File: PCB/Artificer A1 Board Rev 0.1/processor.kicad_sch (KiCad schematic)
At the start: 1 part, among them U1 T527M00X0DCH

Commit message: schematic update
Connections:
- net DP: now reaches U1.A24 (USB0-DP)
- net DM: now reaches U1.B24 (USB0-DM)
- net USB1-DP: now reaches U1.D24 (USB1-DP)
- net USB1-DM: now reaches U1.E24 (USB1-DM)
- net PCIE-TX0-DP/USB3-TXP : now reaches U1.A22 (PCIETX0-DP/USB)
- net PCIE-REF-CLKP: now reaches U1.B21 (PCIEREFCLKP)
- net PCIE-TX0-DN/USB3-TXN: now reaches U1.B22 (PCIETX0-DN/USB)
- net PCIE-RX0-DP/USB3-RXP: now reaches U1.B23 (PCIERX0-DP/US)
- net PCIE-REF-CLKN: now reaches U1.C21 (PCIEREFCLKN)
- net PCIE-RX0-DN/USB3-RXN: now reaches U1.C23 (PCIERX0-DN/US)
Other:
- moved on the sheet: U1D

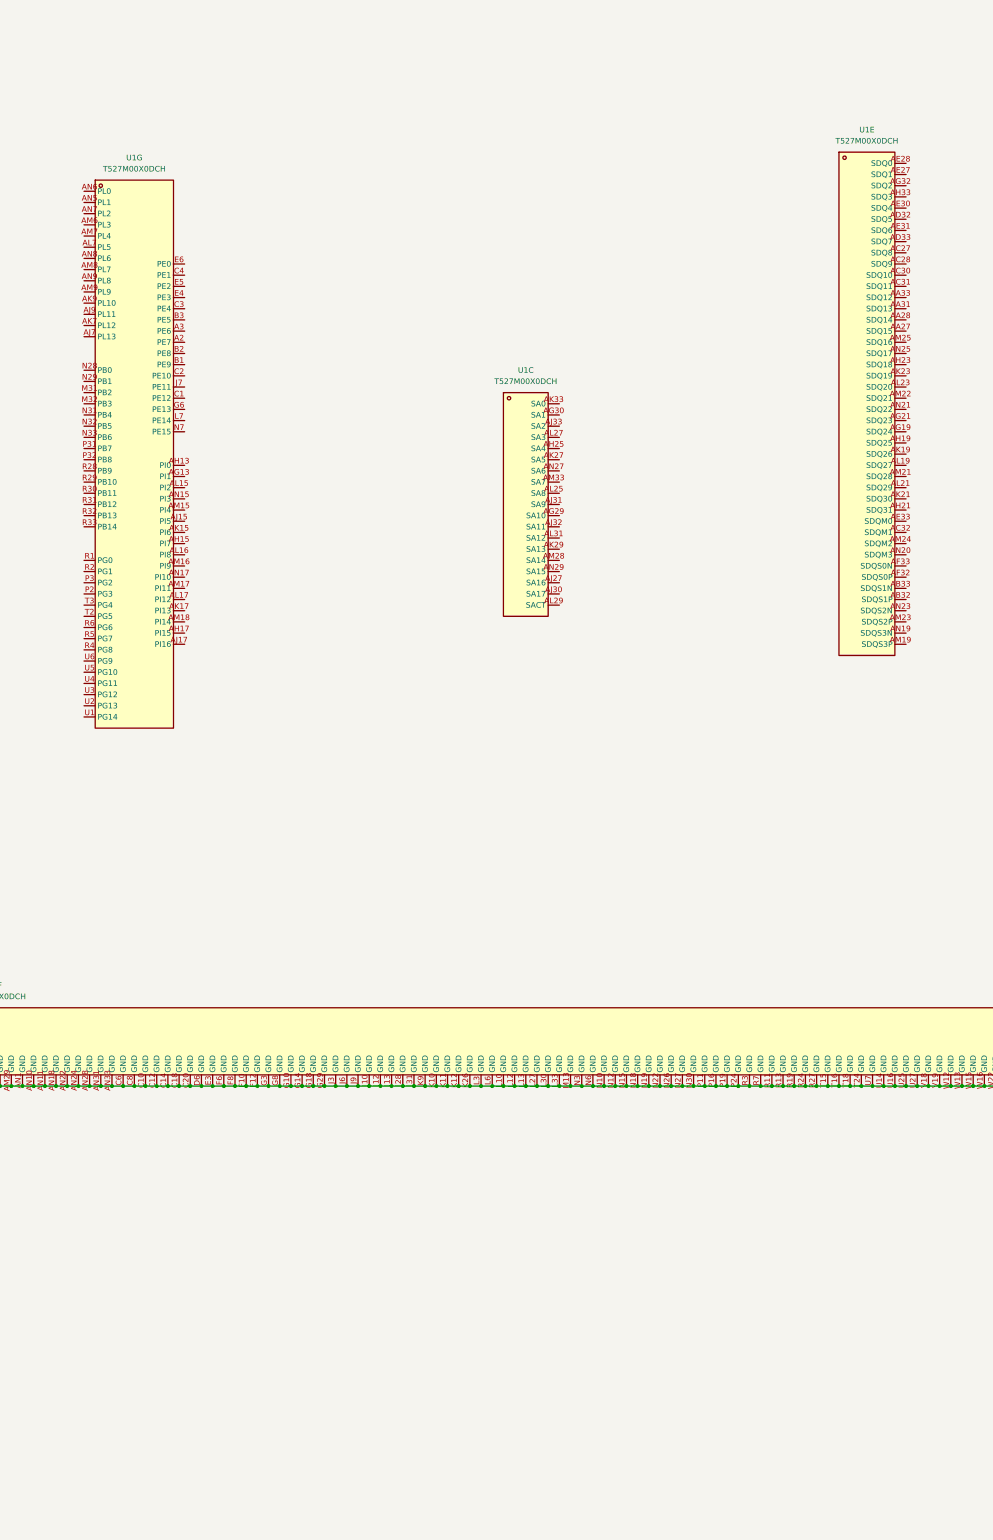
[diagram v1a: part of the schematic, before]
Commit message: localized libraries
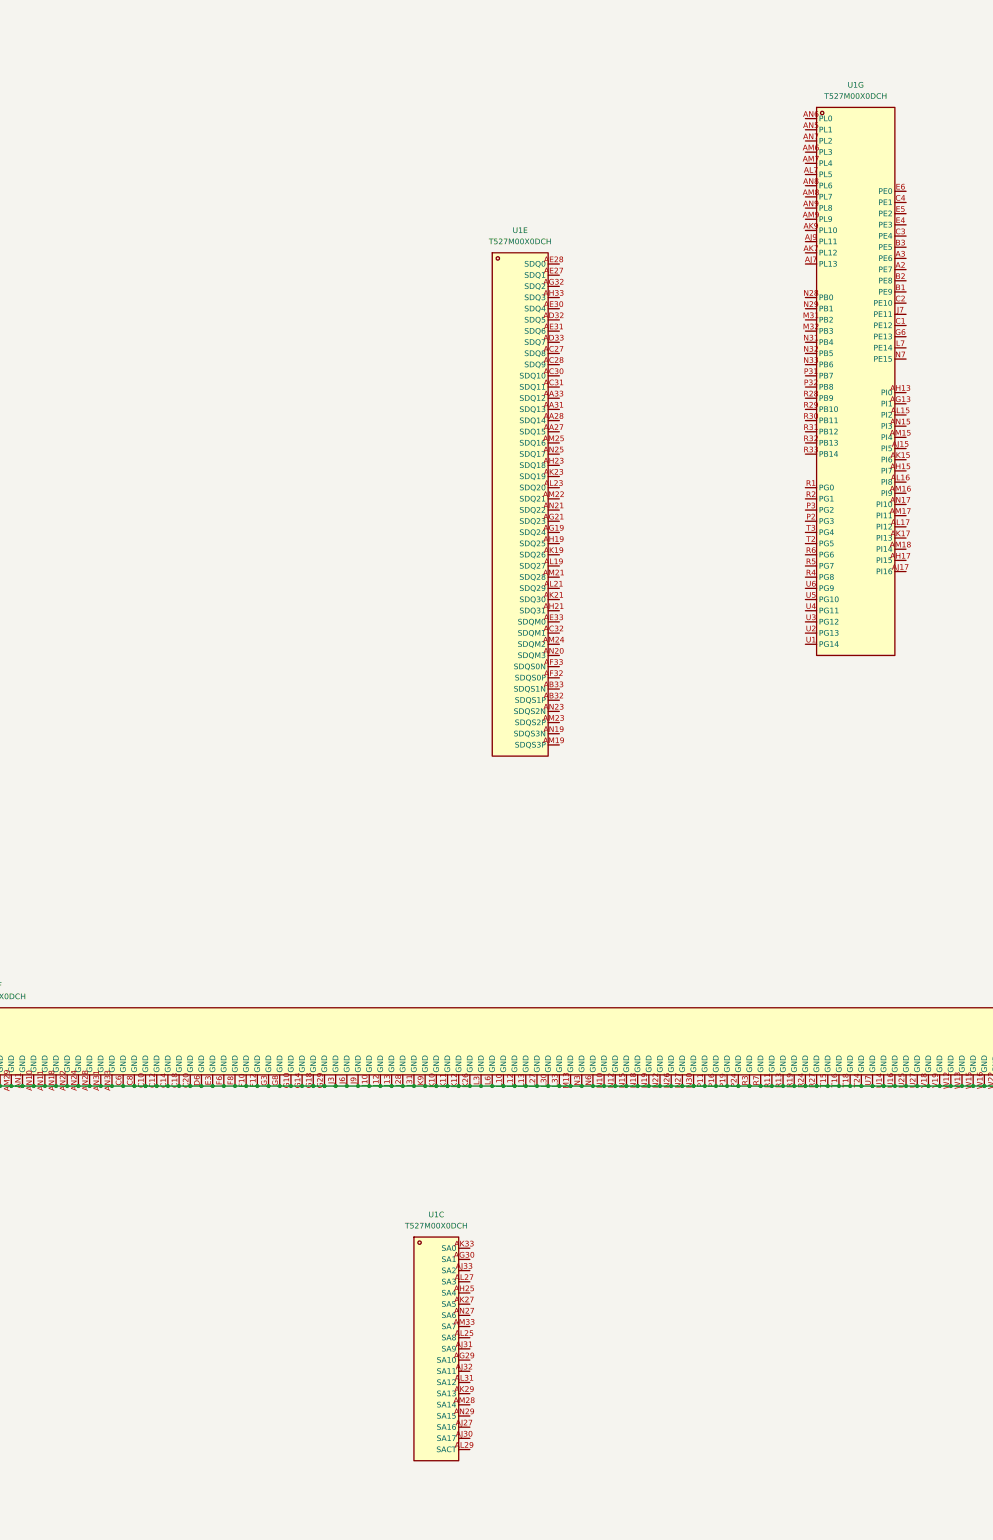
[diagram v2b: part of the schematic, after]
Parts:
- removed U1: T527M00X0DCH, easyeda2kicad:BGA-664_L17.0-W17.0_T527, symbol easyeda2kicad:T527M00X0DCH
- added U1: T527M00X0DCH, easyeda:BGA-664_L17.0-W17.0_T527, symbol easyeda:T527M00X0DCH
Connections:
- net AGND: now also U1.AE3 (AGND)
- net AVSS: now also U1.A32 (AVSS), U1.A33 (AVSS), U1.C22 (AVSS), U1.C24 (AVSS), U1.C26 (AVSS), U1.C28 (AVSS), U1.C30 (AVSS), U1.C31 (AVSS), U1.E29 (AVSS), U1.F22 (AVSS), U1.F24 (AVSS), U1.G26 (AVSS), U1.G28 (AVSS), U1.H24 (AVSS), U1.J17 (AVSS), U1.J21 (AVSS), U1.J22 (AVSS), U1.J23 (AVSS), U1.J26 (AVSS), U1.K15 (AVSS), U1.K16 (AVSS), U1.K21 (AVSS), U1.K22 (AVSS), U1.K24 (AVSS), U1.K25 (AVSS), U1.L16 (AVSS), U1.L19 (AVSS), U1.L24 (AVSS), U1.M16 (AVSS), U1.M18 (AVSS), U1.M19 (AVSS)
- net DM: now also U1.B24 (USB0-DM)
- net DP: now also U1.A24 (USB0-DP)
- net GND: now also U1.A1 (GND), U1.AA15 (GND), U1.AA16 (GND), U1.AA18 (GND), U1.AA21 (GND), U1.AA22 (GND), U1.AA26 (GND), U1.AA30 (GND), U1.AA32 (GND), U1.AB10 (GND), U1.AB11 (GND), U1.AB12 (GND), U1.AB14 (GND), U1.AB15 (GND), U1.AB17 (GND), U1.AC1 (GND), U1.AC26 (GND), U1.AC29 (GND), U1.AC33 (GND), U1.AD11 (GND), U1.AD13 (GND), U1.AD14 (GND), U1.AD20 (GND), U1.AD21 (GND), U1.AD22 (GND), U1.AD9 (GND), U1.AE12 (GND), U1.AE14 (GND), U1.AE18 (GND), U1.AE19 (GND), U1.AE20 (GND), U1.AE21 (GND), U1.AE22 (GND), U1.AE23 (GND), U1.AE24 (GND), U1.AE25 (GND), U1.AE26 (GND), U1.AE29 (GND), U1.AE32 (GND), U1.AE9 (GND), U1.AG11 (GND), U1.AG25 (GND), U1.AG28 (GND), U1.AG3 (GND), U1.AG31 (GND), U1.AG33 (GND), U1.AG6 (GND), U1.AG7 (GND), U1.AH27 (GND), U1.AH32 (GND), U1.AH7 (GND), U1.AH9 (GND), U1.AJ13 (GND), U1.AJ19 (GND), U1.AJ21 (GND), U1.AJ23 (GND), U1.AK11 (GND), U1.AK32 (GND), U1.AK5 (GND), U1.AL12 (GND), U1.AL13 (GND), U1.AL14 (GND), U1.AL3 (GND), U1.AL9 (GND), U1.AM20 (GND), U1.AM26 (GND), U1.AM29 (GND), U1.AM5 (GND), U1.AN1 (GND), U1.AN10 (GND), U1.AN11 (GND), U1.AN18 (GND), U1.AN22 (GND), U1.AN24 (GND), U1.AN28 (GND), U1.AN31 (GND), U1.AN33 (GND), U1.C10 (GND), U1.C12 (GND), U1.C14 (GND), U1.C18 (GND), U1.C20 (GND), U1.C6 (GND), U1.C8 (GND), U1.D6 (GND), U1.E3 (GND), U1.F10 (GND), U1.F12 (GND), U1.F6 (GND), U1.F8 (GND), U1.G10 (GND), U1.G14 (GND), U1.G18 (GND), U1.G29 (GND), U1.G3 (GND), U1.G8 (GND), U1.J10 (GND), U1.J12 (GND), U1.J13 (GND), U1.J28 (GND), U1.J3 (GND), U1.J31 (GND), U1.J6 (GND), U1.J9 (GND), U1.K10 (GND), U1.K11 (GND), U1.K12 (GND), U1.K26 (GND), U1.K9 (GND), U1.L10 (GND), U1.L12 (GND), U1.L13 (GND), U1.L27 (GND), U1.L3 (GND), U1.L30 (GND), U1.L33 (GND), U1.L6 (GND), U1.M13 (GND), U1.N10 (GND), U1.N12 (GND), U1.N15 (GND), U1.N18 (GND), U1.N19 (GND), U1.N22 (GND), U1.N26 (GND), U1.N27 (GND), U1.N3 (GND), U1.N30 (GND), U1.N6 (GND), U1.P11 (GND), U1.P16 (GND), U1.P19 (GND), U1.P24 (GND), U1.R11 (GND), U1.R13 (GND), U1.R19 (GND), U1.R24 (GND), U1.R27 (GND), U1.R3 (GND), U1.R7 (GND), U1.T15 (GND), U1.T16 (GND), U1.T18 (GND), U1.T24 (GND), U1.U14 (GND), U1.U16 (GND), U1.U25 (GND), U1.U27 (GND), U1.U7 (GND), U1.V18 (GND), U1.V19 (GND), U1.W12 (GND), U1.W13 (GND), U1.W15 (GND), U1.W16 (GND), U1.W22 (GND), U1.W27 (GND), U1.W30 (GND), U1.Y15 (GND), U1.Y18 (GND), U1.Y22 (GND), U1.Y23 (GND), U1.Y26 (GND)
- net GNDADC: now also U1.AA7 (GNDADC)
- net PCIE-REF-CLKN: now also U1.C21 (PCIEREFCLKN)
- net PCIE-REF-CLKP: now also U1.B21 (PCIEREFCLKP)
- net PCIE-RX0-DN/USB3-RXN: now also U1.C23 (PCIERX0-DN/US)
- net PCIE-RX0-DP/USB3-RXP: now also U1.B23 (PCIERX0-DP/US)
- net PCIE-TX0-DN/USB3-TXN: now also U1.B22 (PCIETX0-DN/USB)
- net PCIE-TX0-DP/USB3-TXP : now also U1.A22 (PCIETX0-DP/USB)
- net USB1-DM: now also U1.E24 (USB1-DM)
- net USB1-DP: now also U1.D24 (USB1-DP)
- new net: U1.AA12 (VDDDNR), U1.AA13 (VDDDNR), U1.Y12 (VDDDNR), U1.Y13 (VDDDNR)
- new net: U1.AA24 (VCCDRAM), U1.AB24 (VCCDRAM), U1.AC24 (VCCDRAM), U1.W23 (VCCDRAM), U1.W24 (VCCDRAM), U1.W25 (VCCDRAM), U1.Y24 (VCCDRAM)
- new net: U1.AC17 (VCCDRAML), U1.AC18 (VCCDRAML), U1.AC19 (VCCDRAML), U1.AC20 (VCCDRAML), U1.AC22 (VCCDRAML)
- new net: U1.N21 (VDDDE), U1.P21 (VDDDE)
- new net: U1.T11 (VDDGPU), U1.T13 (VDDGPU), U1.U12 (VDDGPU), U1.U13 (VDDGPU)
- new net: U1.T19 (VDDCPUB), U1.T21 (VDDCPUB), U1.T22 (VDDCPUB), U1.U18 (VDDCPUB), U1.U19 (VDDCPUB), U1.U21 (VDDCPUB), U1.U22 (VDDCPUB)
- new net: U1.W19 (VDDCPUL), U1.W21 (VDDCPUL), U1.Y19 (VDDCPUL), U1.Y21 (VDDCPUL)

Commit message: added a few accessories
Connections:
- net MCSIA-CKN: now reaches U1.A10 (PK4)
- net MCSIA-D0N: now reaches U1.A12 (PK0)
- net RGMII0-TXD2: now reaches U1.A14 (PH18)
- net MCSID-CKN: now reaches U1.A4 (PK22)
- net MCSID-D1N: now reaches U1.A5 (PK20)
- net MCSID-D0N: now reaches U1.A6 (PK18)
- net MCSIC-D1N: now reaches U1.A8 (PK14)
- net MCSIA-CKP: now reaches U1.B10 (PK5)
- net MCSIA-D1N: now reaches U1.B11 (PK2)
- net MCSIA-D0P: now reaches U1.B12 (PK1)
- net RGMII0-TXD3: now reaches U1.B13 (PH17)
- net RGMII0-RXCK: now reaches U1.B14 (PH16)
- net RGMII0-MDIO: now reaches U1.B16 (PH10)
- net RGMII0-TXD1: now reaches U1.B17 (PH4)
- net MCSID-CKP: now reaches U1.B4 (PK23)
- net MCSID-D1P: now reaches U1.B5 (PK21)
- net MCSID-D0P: now reaches U1.B6 (PK19)
- net MCSIC-CKN: now reaches U1.B7 (PK16)
- net MCSIC-D1P: now reaches U1.B8 (PK15)
- net MCSIC-D0N: now reaches U1.B9 (PK12)
- net MCSIA-D1P: now reaches U1.C11 (PK3)
- net RGMII0-MDC: now reaches U1.C16 (PH9)
- net RGMII0-CLKIN: now reaches U1.C17 (PH3)
- net MCSIC-CKP: now reaches U1.C7 (PK17)
- net MCSIC-D0P: now reaches U1.C9 (PK13)
- net RGMII1-RXD1: now reaches U1.D1 (PJ0)
- net MCSIB-D1P: now reaches U1.D10 (PK9)
- net MCSIB-D0P: now reaches U1.D12 (PK7)
- net RGMII0-RXD2: now reaches U1.D14 (PH15)
- net RGMII0-RXCTL: now reaches U1.D18 (PH2)
- net RGMII1-RXD0: now reaches U1.D2 (PJ1)
- net RGMII1-RXD0: now also U1.F2 (PJ5)
- net MCSIB-CKP: now reaches U1.D8 (PK11)
- net RGMII1-RXCTL: now reaches U1.E1 (PJ2)
- net MCSIB-D1N: now reaches U1.E10 (PK8)
- net MCSIB-D0N: now reaches U1.E12 (PK6)
- net RGMII0-RXD3: now reaches U1.E14 (PH14)
- net RGMII0-TXD0: now reaches U1.E16 (PH5)
- net RGMII0-RXD0: now reaches U1.E18 (PH1)
- net RGMII1-CLKIN: now reaches U1.E2 (PJ3)
- net MCSIB-CKN: now reaches U1.E8 (PK10)
- net RGMII1-TXD1: now reaches U1.F1 (PJ4)
- net RGMII0-TXCTL: now reaches U1.F14 (PH7)
- net RGMII0-RXD1: now reaches U1.F18 (PH0)
- net RGMII1-TXCK: now reaches U1.G1 (PJ6)
- net RGMII0-TXCK: now reaches U1.G12 (PH6)
- net RGMII1-TXCTL: now reaches U1.G2 (PJ7)
- net RGMII1-RXD3: now reaches U1.G5 (PJ11)
- net RGMII1-MDC: now reaches U1.H2 (PJ8)
- net RGMII1-MDIO: now reaches U1.H3 (PJ9)
- net RGMII1-RXD2: now reaches U1.J4 (PJ12)
- net RGMII1-RXCK: now reaches U1.J5 (PJ13)
- net RGMII1-TXD3: now reaches U1.L4 (PJ14)
- net RGMII1-TXD2: now reaches U1.L5 (PJ15)
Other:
- moved on the sheet: U1A, U1D, U1E, U1G

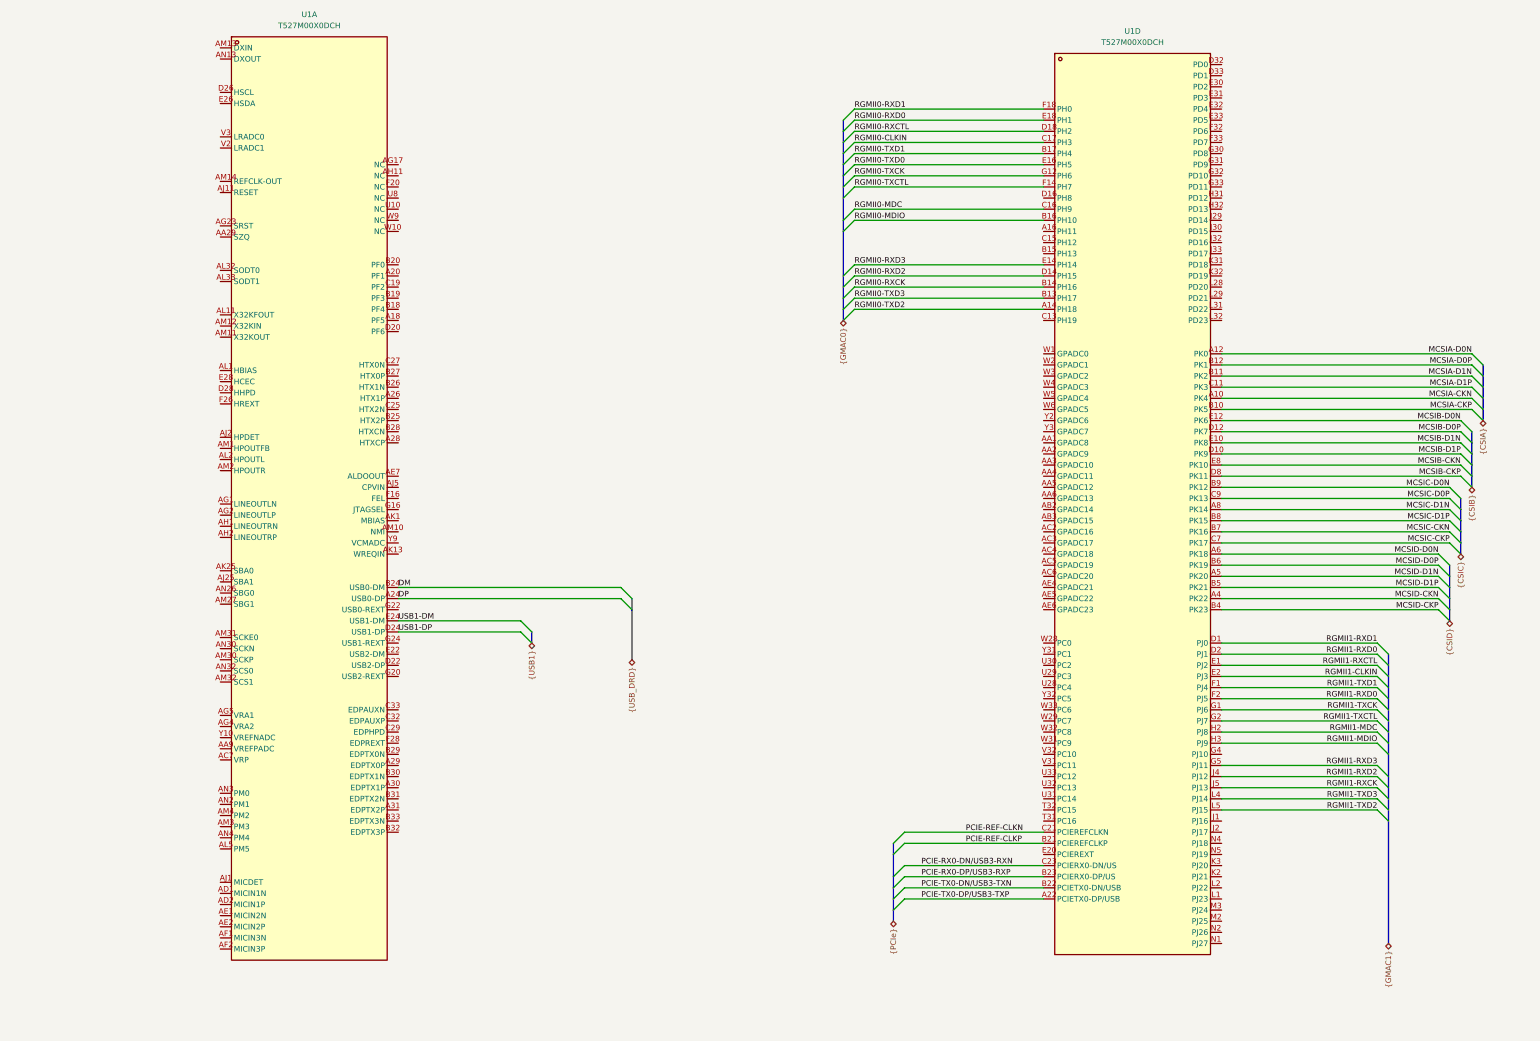
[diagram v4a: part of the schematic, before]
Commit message: added HDMI, DP, DSI, etc
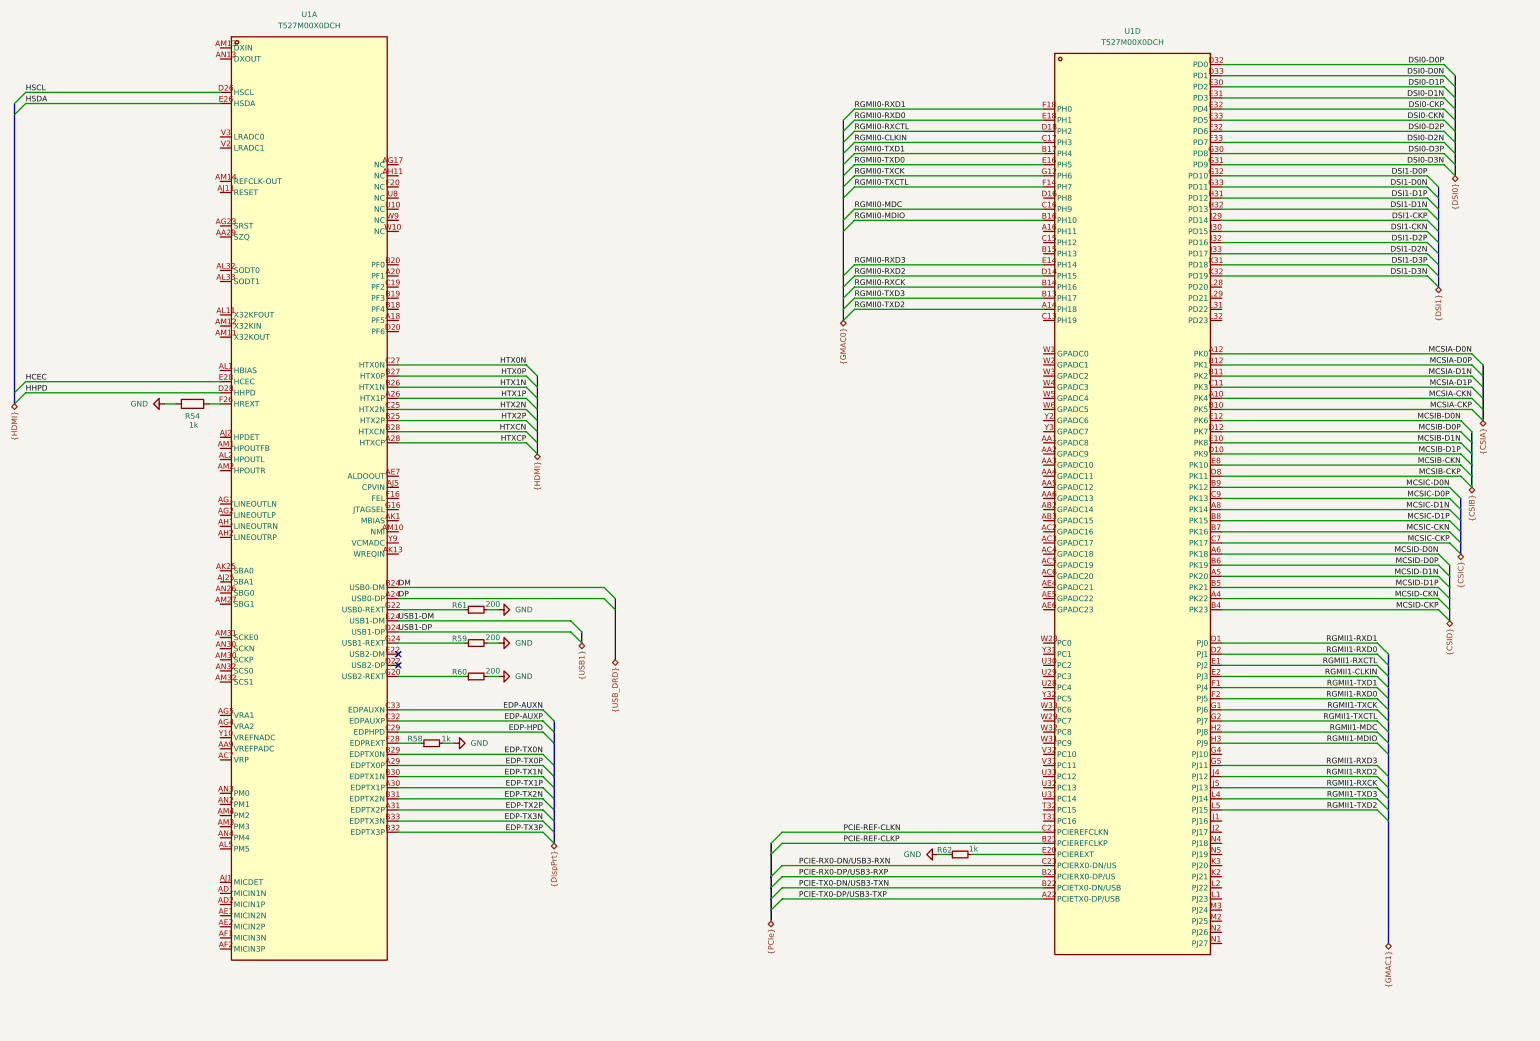
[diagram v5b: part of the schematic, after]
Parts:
- added R54: 1k, symbol Device:R
- added R58, R62: 1k, symbol Device:R_Small
- added R59, R60, R61: 200, symbol Device:R_Small
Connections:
- net GND: now also R54.1, R58.2, R59.2, R60.2, R61.2, R62.1
- net DSI0-D0P: now reaches U1.D32 (PD0)
- net DSI0-D0N: now reaches U1.D33 (PD1)
- net at U1.E20 (PCIEREXT): now also R62.2
- net DSI0-D1P: now reaches U1.E30 (PD2)
- net DSI0-D1N: now reaches U1.E31 (PD3)
- net DSI0-CKP: now reaches U1.E32 (PD4)
- net DSI0-CKN: now reaches U1.E33 (PD5)
- net DSI0-D2P: now reaches U1.F32 (PD6)
- net DSI0-D2N: now reaches U1.F33 (PD7)
- net DSI0-D3P: now reaches U1.G30 (PD8)
- net DSI0-D3N: now reaches U1.G31 (PD9)
- net DSI1-D0P: now reaches U1.G32 (PD10)
- net DSI1-D0N: now reaches U1.G33 (PD11)
- net DSI1-D1P: now reaches U1.H31 (PD12)
- net DSI1-D1N: now reaches U1.H32 (PD13)
- net DSI1-CKP: now reaches U1.J29 (PD14)
- net DSI1-CKN: now reaches U1.J30 (PD15)
- net DSI1-D2P: now reaches U1.J32 (PD16)
- net DSI1-D2N: now reaches U1.J33 (PD17)
- net DSI1-D3P: now reaches U1.K31 (PD18)
- net DSI1-D3N: now reaches U1.K32 (PD19)
- net HTX1P: now reaches U1.A26 (HTX1P)
- net HTXCP: now reaches U1.A28 (HTXCP)
- net EDP-TX0P: now reaches U1.A29 (EDPTX0P)
- net EDP-TX1P: now reaches U1.A30 (EDPTX1P)
- net EDP-TX2P: now reaches U1.A31 (EDPTX2P)
- net HTX2P: now reaches U1.B25 (HTX2P)
- net HTX1N: now reaches U1.B26 (HTX1N)
- net HTX0P: now reaches U1.B27 (HTX0P)
- net HTXCN: now reaches U1.B28 (HTXCN)
- net EDP-TX0N: now reaches U1.B29 (EDPTX0N)
- net EDP-TX1N: now reaches U1.B30 (EDPTX1N)
- net EDP-TX2N: now reaches U1.B31 (EDPTX2N)
- net EDP-TX3P: now reaches U1.B32 (EDPTX3P)
- net EDP-TX3N: now reaches U1.B33 (EDPTX3N)
- net HTX2N: now reaches U1.C25 (HTX2N)
- net HTX0N: now reaches U1.C27 (HTX0N)
- net EDP-HPD: now reaches U1.C29 (EDPHPD)
- net EDP-AUXP: now reaches U1.C32 (EDPAUXP)
- net EDP-AUXN: now reaches U1.C33 (EDPAUXN)
- net HSCL: now reaches U1.D26 (HSCL)
- net HHPD: now reaches U1.D28 (HHPD)
- net HSDA: now reaches U1.E26 (HSDA)
- net HCEC: now reaches U1.E28 (HCEC)
- net at U1.F26 (HREXT): now also R54.2
- net at U1.F28 (EDPREXT): now also R58.1
- net at U1.G20 (USB2-REXT): now also R60.1
- net at U1.G22 (USB0-REXT): now also R61.1
- net at U1.G24 (USB1-REXT): now also R59.1
- no-connect marks 0 -> 2

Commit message: finished dram
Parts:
- removed unit 3 of U1
- removed unit 5 of U1
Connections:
- net AVSS is gone; now on net GND: U1.A32 (AVSS), U1.A33 (AVSS), U1.C22 (AVSS), U1.C24 (AVSS), U1.C26 (AVSS), U1.C28 (AVSS), U1.C30 (AVSS), U1.C31 (AVSS), U1.E29 (AVSS), U1.F22 (AVSS), U1.F24 (AVSS), U1.G26 (AVSS), U1.G28 (AVSS), U1.H24 (AVSS), U1.J17 (AVSS), U1.J21 (AVSS), U1.J22 (AVSS), U1.J23 (AVSS), U1.J26 (AVSS), U1.K15 (AVSS), U1.K16 (AVSS), U1.K21 (AVSS), U1.K22 (AVSS), U1.K24 (AVSS), U1.K25 (AVSS), U1.L16 (AVSS), U1.L19 (AVSS), U1.L24 (AVSS), U1.M16 (AVSS), U1.M18 (AVSS), U1.M19 (AVSS)
- net VDD11-DRAM: now reaches U1.AA24 (VCCDRAM), U1.AB24 (VCCDRAM), U1.AC24 (VCCDRAM), U1.W23 (VCCDRAM), U1.W24 (VCCDRAM), U1.W25 (VCCDRAM), U1.Y24 (VCCDRAM)
- net VDD06-DRAM: now reaches U1.AC17 (VCCDRAML), U1.AC18 (VCCDRAML), U1.AC19 (VCCDRAML), U1.AC20 (VCCDRAML), U1.AC22 (VCCDRAML)
- net VDD18-DRAM: now reaches U1.AD25 (VDD18-DRAM)
- net AGND: no longer names the net of U1.AE3 (AGND)
- net GNDADC: no longer names the net of U1.AA7 (GNDADC)
- no-connect marks 2 -> 9
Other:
- moved on the sheet: R54, R58, R59, R60, R61, R62, U1B, U1D, U1F

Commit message: added: sd, wifi, audio, started power, fixed buses
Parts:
- removed unit 2 of U1
- removed unit 6 of U1
- added R74: 1k, symbol Device:R_Small
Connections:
- net SDC0-D2: now reaches U1.A18 (PF5)
- net SDC0-D0: now reaches U1.A20 (PF1)
- net MICIN3N: now reaches U1.AF1 (MICIN3N)
- net MICIN3P: now reaches U1.AF2 (MICIN3P)
- net at U1.AJ1 (MICDET): now also R74.2
- net HP-DET: now reaches U1.AJ2 (HPDET)
- net HBIAS: now reaches U1.AL1 (HBIAS)
- net HPOUTL: now reaches U1.AL2 (HPOUTL)
- net HPOUTFB: now reaches U1.AM1 (HPOUTFB)
- net HPOUTR: now reaches U1.AM2 (HPOUTR)
- net WL-WAKE-AP: now reaches U1.AM3 (PM3)
- net AP-WAKE-WL: now reaches U1.AM4 (PM2)
- net BT-WAKE-AP: now reaches U1.AN2 (PM1)
- net AP-WAKE-BT: now reaches U1.AN3 (PM0)
- net PWR-EN: now reaches U1.AN4 (PM4)
- net SDC0-D3: now reaches U1.B18 (PF4)
- net SDC0-CMD: now reaches U1.B19 (PF3)
- net SDC0-D1: now reaches U1.B20 (PF0)
- net SDC0-CLK: now reaches U1.C19 (PF2)
- net SDC0-DET: now reaches U1.D20 (PF6)
- net SDC1-D1: now reaches U1.P2 (PG3)
- net SDC1-D0: now reaches U1.P3 (PG2)
- net SDC1-CLK: now reaches U1.R1 (PG0)
- net SDC1-CMD: now reaches U1.R2 (PG1)
- net BT-UART-RTS: now reaches U1.R4 (PG8)
- net BT-UART-RX: now reaches U1.R5 (PG7)
- net BT-UART-TX: now reaches U1.R6 (PG6)
- net SDC1-D3: now reaches U1.T2 (PG5)
- net SDC1-D2: now reaches U1.T3 (PG4)
- net BT-PCM-DIN: now reaches U1.U1 (PG14)
- net BT-PCM-DOUT: now reaches U1.U2 (PG13)
- net BT-PCM-SYNC: now reaches U1.U3 (PG12)
- net BT-PCM-CLK: now reaches U1.U4 (PG11)
- net BT-UART-CTS: now reaches U1.U6 (PG9)
- net PCIE-RX0-DN/USB3-RXN renamed PCIE-RX0-DN
- net PCIE-RX0-DP/USB3-RXP renamed PCIE-RX0-DP
- net PCIE-TX0-DN/USB3-TXN renamed PCIE-TX0-DN
- net PCIE-TX0-DP/USB3-TXP  renamed PCIE-TX0-DP
- new net HS-MIC: R74.1
- no-connect marks 9 -> 10
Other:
- moved on the sheet: U1G
